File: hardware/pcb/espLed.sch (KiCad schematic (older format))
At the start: 15 parts, among them Q1 IRF9310TRPBF, U1 AMS1117-3.3

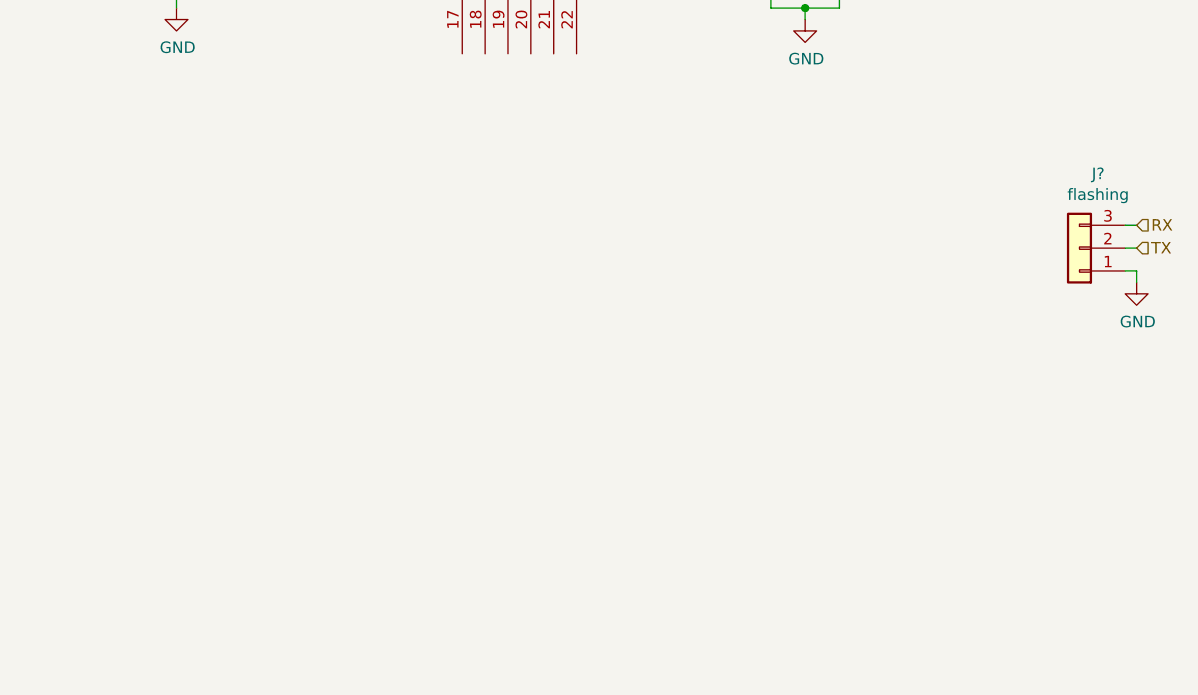
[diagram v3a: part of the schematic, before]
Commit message: layout mosfets and add a connector for the led strip
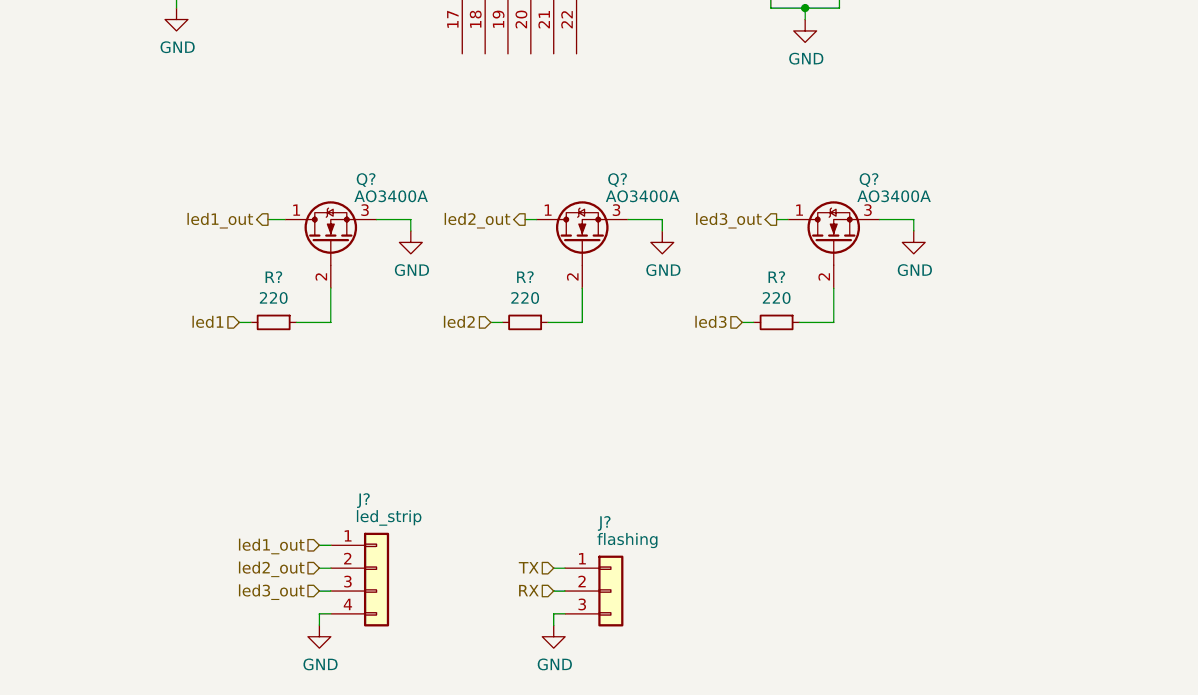
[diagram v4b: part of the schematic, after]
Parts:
- added J?: led_strip, symbol Connector_Generic:Conn_01x04
- added Q? (x3): AO3400A, Package_TO_SOT_SMD:SOT-23, symbol Device:Q_NMOS_DGS
- added R? (x3): 220, Resistor_SMD:R_0805_2012Metric, symbol Device:R_Small
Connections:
- net GND: now also J?.3 (Pin_3), J?.4 (Pin_4), Q?.3 (S), Q?.3 (S), Q?.3 (S); no longer J?.1 (Pin_1)
- net RX: now also J?.2 (Pin_2); no longer J?.3 (Pin_3)
- net TX: now also J?.1 (Pin_1); no longer J?.2 (Pin_2)
- net led1: now also R?.2
- net led2: now also R?.2
- net led3: now also R?.2
- new net: Q?.2 (G), R?.1 (x3)
- new net led1_out: J?.1 (Pin_1), Q?.1 (D)
- new net led2_out: J?.2 (Pin_2), Q?.1 (D)
- new net led3_out: J?.3 (Pin_3), Q?.1 (D)
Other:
- moved on the sheet: J?
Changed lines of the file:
@@
 Wire Wire Line
 	9200 1500 8600 1500
-Wire Wire Line
-	10400 3350 10350 3350
-Wire Wire Line
-	10400 3400 10400 3350
 $Comp
 L power:GND #PWR?
 U 1 1 6009ECDE
-P 10400 3400
-F 0 "#PWR?" H 10400 3150 50  0001 C CNN
-F 1 "GND" H 10405 3227 50  0000 C CNN
-F 2 "" H 10400 3400 50  0001 C CNN
-F 3 "" H 10400 3400 50  0001 C CNN
-	1    10400 3400
-	1    0    0    -1
-$EndComp
-Wire Wire Line
-	10400 3250 10350 3250
-Text HLabel 10400 3250 2    50   Input ~ 0
+P 7850 4900
+F 0 "#PWR?" H 7850 4650 50  0001 C CNN
+F 1 "GND" H 7855 4727 50  0000 C CNN
+F 2 "" H 7850 4900 50  0001 C CNN
+F 3 "" H 7850 4900 50  0001 C CNN
+	1    7850 4900
+	1    0    0    -1
+$EndComp
+Wire Wire Line
+	7850 4750 7900 4750
+Text HLabel 7850 4650 0    50   Input ~ 0
 TX
-Wire Wire Line
-	10400 3150 10350 3150
-Text HLabel 10400 3150 2    50   Input ~ 0
+Text HLabel 7850 4750 0    50   Input ~ 0
 RX
 $Comp
 L Connector_Generic:Conn_01x03 J?
 U 1 1 6009A6C5
-P 10150 3250
-F 0 "J?" H 10068 2925 50  0000 C CNN
-F 1 "flashing" H 10068 3016 50  0000 C CNN
-F 2 "" H 10150 3250 50  0001 C CNN
-F 3 "~" H 10150 3250 50  0001 C CNN
-	1    10150 3250
-	-1   0    0    1
-$EndComp
+P 8100 4750
+F 0 "J?" H 8075 5050 50  0000 C CNN
+F 1 "flashing" H 8175 4975 50  0000 C CNN
+F 2 "" H 8100 4750 50  0001 C CNN
+F 3 "~" H 8100 4750 50  0001 C CNN
+	1    8100 4750
+	1    0    0    -1
+$EndComp
+Text HLabel 6475 3575 0    50   Input ~ 0
+led1
+Wire Wire Line
+	6525 3575 6475 3575
+$Comp
+L Device:R_Small R?
+U 1 1 600C9AA0
+P 6625 3575
+F 0 "R?" V 6429 3575 50  0000 C CNN
+F 1 "220" V 6520 3575 50  0000 C CNN
+F 2 "Resistor_SMD:R_0805_2012Metric" H 6625 3575 50  0001 C CNN
+F 3 "~" H 6625 3575 50  0001 C CNN
+	1    6625 3575
+	0    1    1    0
+$EndComp
+$Comp
+L power:GND #PWR?
+U 1 1 600C49E3
+P 7225 3175
+F 0 "#PWR?" H 7225 2925 50  0001 C CNN
+F 1 "GND" H 7230 3002 50  0000 C CNN
+F 2 "" H 7225 3175 50  0001 C CNN
+F 3 "" H 7225 3175 50  0001 C CNN
+	1    7225 3175
+	1    0    0    -1
+$EndComp
+Wire Wire Line
+	7225 3175 7225 3125
+Wire Wire Line
+	7075 3125 7225 3125
+Wire Wire Line
+	6725 3575 6875 3575
+Wire Wire Line
+	6875 3425 6875 3575
+$Comp
+L Device:Q_NMOS_DGS Q?
+U 1 1 600BF2DA
+P 6875 3225
+F 0 "Q?" V 7150 3025 50  0000 L CNN
+F 1 "AO3400A" V 7075 2800 50  0000 L CNN
+F 2 "Package_TO_SOT_SMD:SOT-23" H 7075 3325 50  0001 C CNN
+F 3 "https://static.chipdip.ru/lib/046/DOC003046153.pdf" H 6875 3225 50  0001 C CNN
+	1    6875 3225
+	0    -1   -1   0
+$EndComp
+Text HLabel 7575 3575 0    50   Input ~ 0
+led2
+Wire Wire Line
+	7625 3575 7575 3575
+$Comp
+L Device:R_Small R?
+U 1 1 600FDD72
+P 7725 3575
+F 0 "R?" V 7529 3575 50  0000 C CNN
+F 1 "220" V 7620 3575 50  0000 C CNN
+F 2 "Resistor_SMD:R_0805_2012Metric" H 7725 3575 50  0001 C CNN
+F 3 "~" H 7725 3575 50  0001 C CNN
+	1    7725 3575
+	0    1    1    0
+$EndComp
+$Comp
+L power:GND #PWR?
+U 1 1 600FDD78
+P 8325 3175
+F 0 "#PWR?" H 8325 2925 50  0001 C CNN
+F 1 "GND" H 8330 3002 50  0000 C CNN
+F 2 "" H 8325 3175 50  0001 C CNN
+F 3 "" H 8325 3175 50  0001 C CNN
+	1    8325 3175
+	1    0    0    -1
+$EndComp
+Wire Wire Line
+	8325 3175 8325 3125
+Wire Wire Line
+	8175 3125 8325 3125
+Wire Wire Line
+	7825 3575 7975 3575
+Wire Wire Line
+	7975 3425 7975 3575
+$Comp
+L Device:Q_NMOS_DGS Q?
+U 1 1 600FDD82
+P 7975 3225
+F 0 "Q?" V 8250 3025 50  0000 L CNN
+F 1 "AO3400A" V 8175 2800 50  0000 L CNN
+F 2 "Package_TO_SOT_SMD:SOT-23" H 8175 3325 50  0001 C CNN
+F 3 "https://static.chipdip.ru/lib/046/DOC003046153.pdf" H 7975 3225 50  0001 C CNN
+	1    7975 3225
+	0    -1   -1   0
+$EndComp
+Text HLabel 8675 3575 0    50   Input ~ 0
+led3
+Wire Wire Line
+	8725 3575 8675 3575
+$Comp
+L Device:R_Small R?
+U 1 1 60107E5C
+P 8825 3575
+F 0 "R?" V 8629 3575 50  0000 C CNN
+F 1 "220" V 8720 3575 50  0000 C CNN
+F 2 "Resistor_SMD:R_0805_2012Metric" H 8825 3575 50  0001 C CNN
+F 3 "~" H 8825 3575 50  0001 C CNN
+	1    8825 3575
+	0    1    1    0
+$EndComp
+$Comp
+L power:GND #PWR?
+U 1 1 60107E62
+P 9425 3175
+F 0 "#PWR?" H 9425 2925 50  0001 C CNN
+F 1 "GND" H 9430 3002 50  0000 C CNN
+F 2 "" H 9425 3175 50  0001 C CNN
+F 3 "" H 9425 3175 50  0001 C CNN
+	1    9425 3175
+	1    0    0    -1
+$EndComp
+Wire Wire Line
+	9425 3175 9425 3125
+Wire Wire Line
+	9275 3125 9425 3125
+Wire Wire Line
+	8925 3575 9075 3575
+Wire Wire Line
+	9075 3425 9075 3575
+$Comp
+L Device:Q_NMOS_DGS Q?
+U 1 1 60107E6C
+P 9075 3225
+F 0 "Q?" V 9350 3025 50  0000 L CNN
+F 1 "AO3400A" V 9275 2800 50  0000 L CNN
+F 2 "Package_TO_SOT_SMD:SOT-23" H 9275 3325 50  0001 C CNN
+F 3 "https://static.chipdip.ru/lib/046/DOC003046153.pdf" H 9075 3225 50  0001 C CNN
+	1    9075 3225
+	0    -1   -1   0
+$EndComp
+Wire Wire Line
+	6600 3125 6675 3125
+Text HLabel 6600 3125 0    50   Output ~ 0
+led1_out
+Text HLabel 7725 3125 0    50   Output ~ 0
+led2_out
+Wire Wire Line
+	7725 3125 7775 3125
+Text HLabel 8825 3125 0    50   Output ~ 0
+led3_out
+Wire Wire Line
+	8825 3125 8875 3125
+Wire Wire Line
+	6825 4750 6875 4750
+Text HLabel 6825 4750 0    50   Input ~ 0
+led3_out
+Wire Wire Line
+	6825 4550 6875 4550
+Wire Wire Line
+	6825 4650 6875 4650
+Text HLabel 6825 4650 0    50   Input ~ 0
+led2_out
+Text HLabel 6825 4550 0    50   Input ~ 0
+led1_out
+$Comp
+L power:GND #PWR?
+U 1 1 6011AB1B
+P 6825 4900
+F 0 "#PWR?" H 6825 4650 50  0001 C CNN
+F 1 "GND" H 6830 4727 50  0000 C CNN
+F 2 "" H 6825 4900 50  0001 C CNN
+F 3 "" H 6825 4900 50  0001 C CNN
+	1    6825 4900
+	1    0    0    -1
+$EndComp
+$Comp
+L Connector_Generic:Conn_01x04 J?
+U 1 1 6010A276
+P 7075 4650
+F 0 "J?" H 7050 4950 50  0000 R CNN
+F 1 "led_strip" H 7275 4875 50  0000 R CNN
+F 2 "" H 7075 4650 50  0001 C CNN
+F 3 "~" H 7075 4650 50  0001 C CNN
+	1    7075 4650
+	1    0    0    -1
+$EndComp
+Wire Wire Line
+	7850 4650 7900 4650
+Wire Wire Line
+	7850 4900 7850 4850
+Wire Wire Line
+	7850 4850 7900 4850
+Wire Wire Line
+	6825 4900 6825 4850
+Wire Wire Line
+	6825 4850 6875 4850
 $EndSCHEMATC

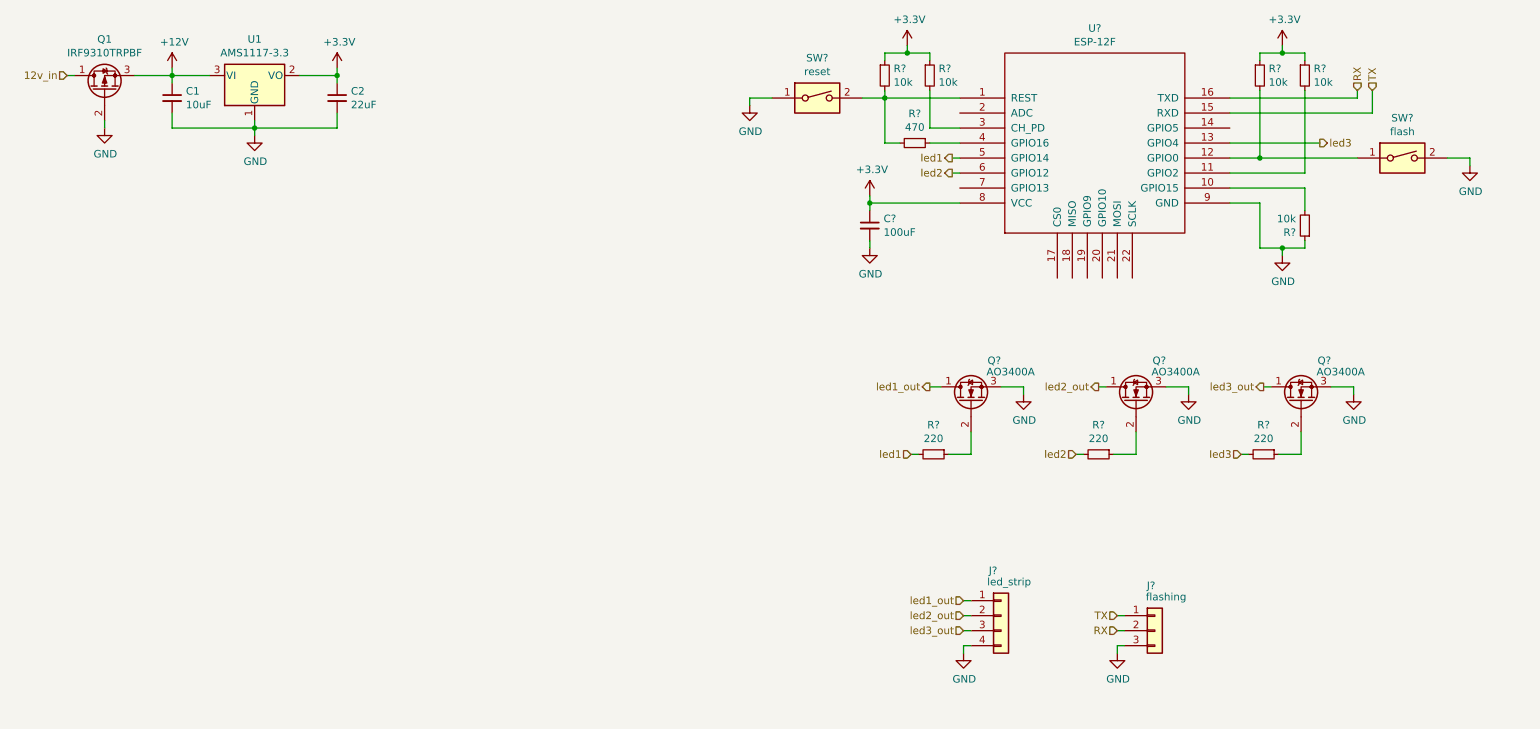
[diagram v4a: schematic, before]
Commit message: layout schematic into block so it looks nice
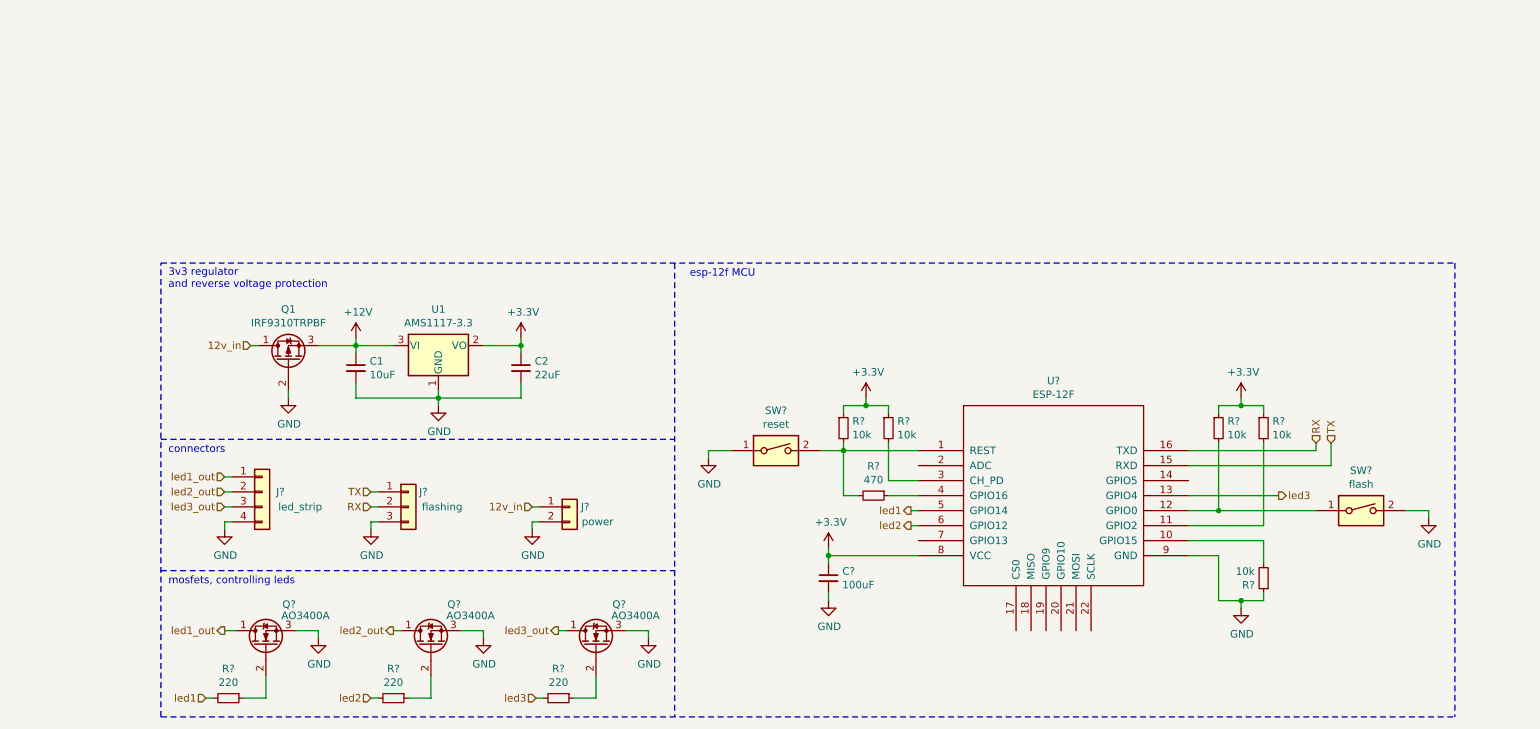
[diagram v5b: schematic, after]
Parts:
- added J?: power, symbol Connector_Generic:Conn_01x02
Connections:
- net 12v_in: now also J?.1 (Pin_1)
- net GND: now also J?.2 (Pin_2)
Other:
- note added: "3v3 regulator\nand reverse voltage protection"
- note added: "connectors"
- note added: "esp-12f MCU"
- note added: "mosfets, controlling leds"
- moved on the sheet: C1, C2, C?, J?, Q1, Q?, R?, SW?, U1, U?

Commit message: assign pcb footprints to the rest of components and annotate schematic
except for the reset button
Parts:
- C1, C2: footprint (none) -> Capacitor_SMD:C_0805_2012Metric
- C3: renamed from C?; footprint (none) -> Capacitor_SMD:C_0805_2012Metric
- J1: renamed from J?; footprint (none) -> Connector_PinSocket_2.54mm:PinSocket_1x04_P2.54mm_Vertical
- J2: renamed from J?; footprint (none) -> Connector_PinSocket_2.54mm:PinSocket_1x03_P2.54mm_Vertical
- J3: renamed from J?; footprint (none) -> Connector_PinSocket_2.54mm:PinSocket_1x02_P2.54mm_Vertical
- R4, R5, R6, R7, R8, R9: renamed from R?; footprint (none) -> Resistor_SMD:R_0805_2012Metric
- SW2: renamed from SW?; footprint (none) -> Connector_PinSocket_2.54mm:PinSocket_1x02_P2.54mm_Vertical
- U2: renamed from U?; footprint (none) -> ESP8266:ESP-12E_SMD
- gave numbers to parts that had none: 7

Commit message: create a footprint for button and assign it to reset
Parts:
- SW1: footprint (none) -> custom:push_button
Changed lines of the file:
@@
 F 0 "SW1" H 5575 3817 50  0000 C CNN
 F 1 "reset" H 5575 3726 50  0000 C CNN
-F 2 "" H 5575 3550 50  0001 C CNN
+F 2 "custom:push_button" H 5575 3550 50  0001 C CNN
 F 3 "~" H 5575 3550 50  0001 C CNN
 	1    5575 3550

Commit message: fix default SO-8 footprint for IRF9310TRPBF mosfet
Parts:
- Q1: footprint Package_SO:HSOP-8-1EP_3.9x4.9mm_P1.27mm_EP2.41x3.1mm -> custom:IRF9310PBF
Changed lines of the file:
@@
 F 0 "Q1" V 2667 2950 50  0000 C CNN
 F 1 "IRF9310TRPBF" V 2576 2950 50  0000 C CNN
-F 2 "Package_SO:HSOP-8-1EP_3.9x4.9mm_P1.27mm_EP2.41x3.1mm" H 2525 3050 50  0001 C CNN
+F 2 "custom:IRF9310PBF" H 2525 3050 50  0001 C CNN
 F 3 "https://static.chipdip.ru/lib/304/DOC004304962.pdf" H 2325 2950 50  0001 C CNN
 	1    2325 2950
